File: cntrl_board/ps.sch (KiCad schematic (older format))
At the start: 52 parts, among them J10 PRI_TRF_L, J11 PRI_TRF_N, J12 SEC_OUT_L, J13 SEC_OUT_N, J6 MAIN_PWR_L, J7 MAIN_PWR_N, J8 SEC_TRF_L, J9 SEC_TRF_N, U1 LM2596S-ADJ, U17 LM1085-ADJ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

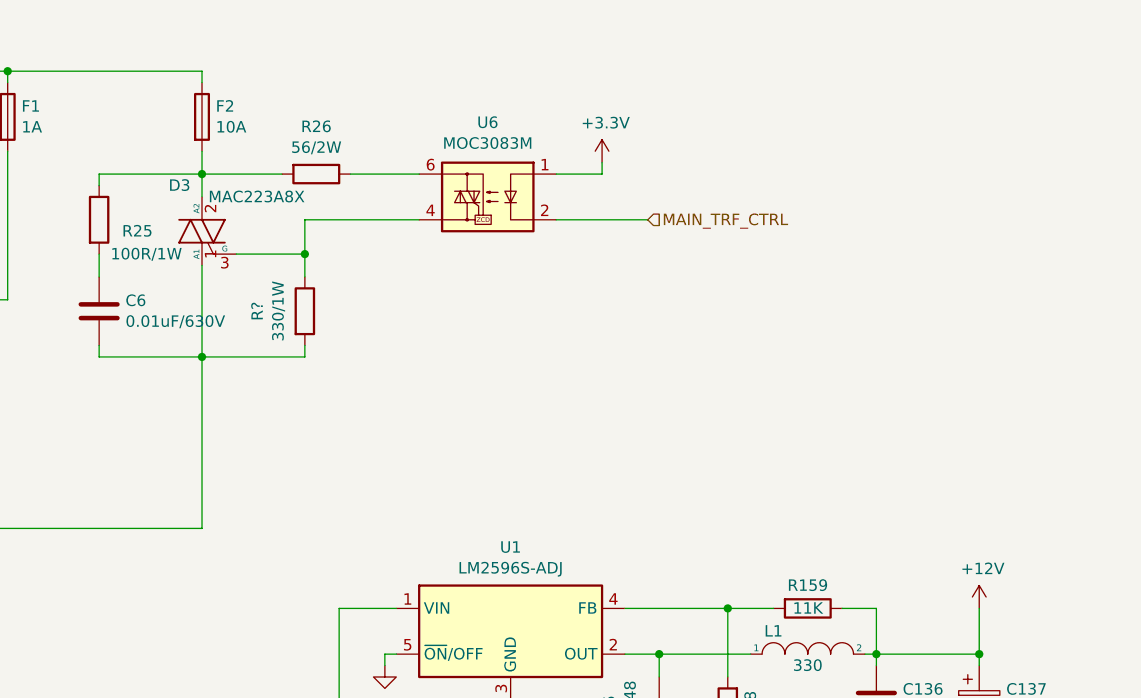
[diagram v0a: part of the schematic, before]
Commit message: update xformer soft startup
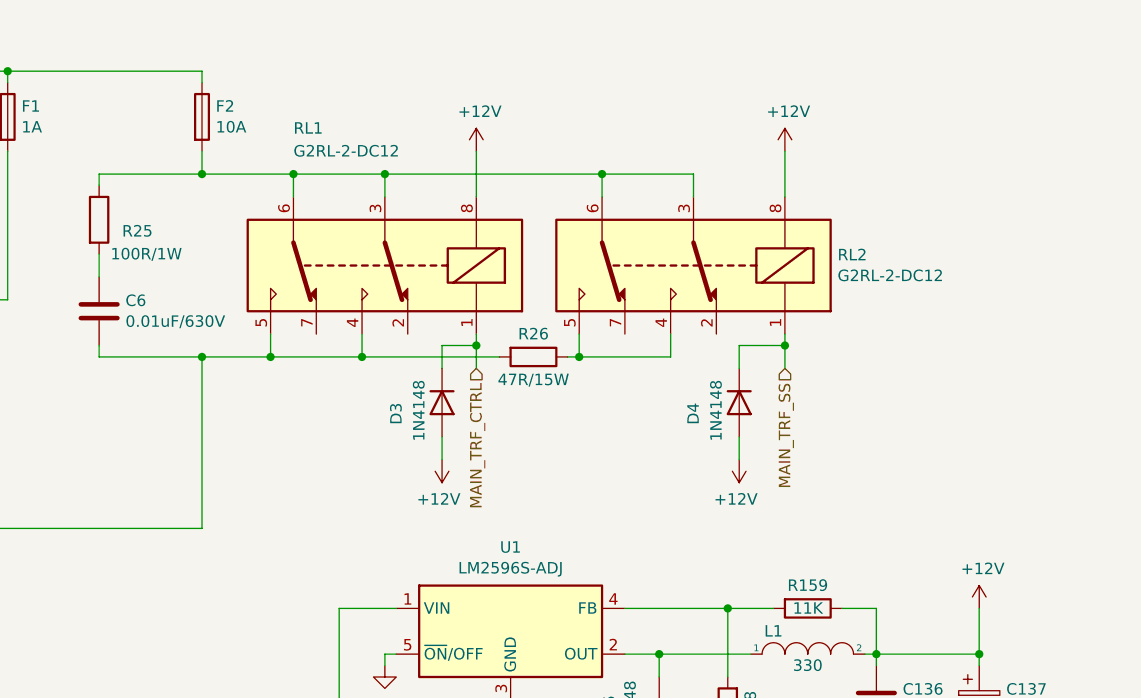
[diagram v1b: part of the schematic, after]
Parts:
- removed D3: MAC223A8X, Package_TO_SOT_THT:TO-220-3_Vertical, symbol Device:Q_TRIAC_A1A2G
- removed R?: 330/1W, Resistor_THT:R_Axial_DIN0414_L11.9mm_D4.5mm_P15.24mm_Horizontal, symbol Device:R
- removed U6: MOC3083M, symbol Relay_SolidState:MOC3083M
- added D3, D4: 1N4148, Diode_SMD:D_SOD-323_HandSoldering, symbol Device:D
- added RL1, RL2: G2RL-2-DC12, Relay_THT:Relay_DPDT_Omron_G2RL, symbol Relay:G2RL-2-DC12
- R26: value 56/2W -> 47R/15W; footprint Resistor_THT:R_Axial_DIN0414_L11.9mm_D4.5mm_P15.24mm_Horizontal -> Resistor_THT:R_Radial_Power_L13.0mm_W9.0mm_P5.00mm
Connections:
- net +12V: now also D3.2 (A), D4.2 (A), RL1.8, RL2.8
- net MAIN_TRF_CTRL: now also D3.1 (K), RL1.1
- net at C6.2, J10.1 (Pin_1): now also R26.2, RL1.4, RL1.5
- net at F2.2, R25.1: now also RL1.3, RL1.6, RL2.3, RL2.6; no longer R26.2
- net at R26.1: now also RL2.4, RL2.5
- new net MAIN_TRF_SS: D4.1 (K), RL2.1
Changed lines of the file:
@@
 $EndDescr
-$Comp
-L Device:Q_TRIAC_A1A2G D3
-U 1 1 60BF28E5
-P 2850 1750
-F 0 "D3" H 2900 1950 50  0000 L CNN
-F 1 "MAC223A8X" H 2400 1900 50  0000 L CNN
-F 2 "Package_TO_SOT_THT:TO-220-3_Vertical" V 2925 1775 50  0001 C CNN
-F 3 "~" V 2850 1750 50  0001 C CNN
-	1    2850 1750
-	-1   0    0    -1
-$EndComp
 $Comp
 L Connector:Conn_01x01_Male J10
@@
 	1    0    0    -1
 $EndComp
-Connection ~ 2850 1500
-Wire Wire Line
-	2850 1500 2850 1600
 Wire Wire Line
 	2400 1850 2400 1950
@@
 	2400 2250 2400 2300
 Wire Wire Line
-	2850 1900 2850 2300
-Wire Wire Line
 	2850 3050 2850 2300
 Wire Wire Line
 	1450 3050 2850 3050
-Connection ~ 2850 2300
 Wire Wire Line
 	2400 2300 2850 2300
@@
 Wire Wire Line
 	2400 1500 2850 1500
-$Comp
-L Device:R R26
-U 1 1 60C0976D
-P 3350 1500
-F 0 "R26" V 3143 1500 50  0000 C CNN
-F 1 "56/2W" V 3234 1500 50  0000 C CNN
-F 2 "Resistor_THT:R_Axial_DIN0414_L11.9mm_D4.5mm_P15.24mm_Horizontal" V 3280 1500 50  0001 C CNN
-F 3 "~" H 3350 1500 50  0001 C CNN
-	1    3350 1500
-	0    1    1    0
-$EndComp
-Wire Wire Line
-	2850 1500 3200 1500
-Wire Wire Line
-	4400 1700 4800 1700
 $Comp
 L Connector:Conn_01x01_Male J12
@@
 	1    0    0    -1
 $EndComp
-Text HLabel 4800 1700 2    50   Input ~ 0
+Text HLabel 4050 2350 3    50   Input ~ 0
 MAIN_TRF_CTRL
 $Comp
@@
 	9500 4950 9650 4950
 $Comp
-L power:+3.3V #PWR0266
-U 1 1 635ACB53
-P 4600 1450
-F 0 "#PWR0266" H 4600 1300 50  0001 C CNN
-F 1 "+3.3V" H 4615 1623 50  0000 C CNN
-F 2 "" H 4600 1450 50  0001 C CNN
-F 3 "" H 4600 1450 50  0001 C CNN
-	1    4600 1450
-	1    0    0    -1
-$EndComp
-Wire Wire Line
-	4600 1500 4600 1450
-Wire Wire Line
-	4400 1500 4600 1500
-$Comp
 L power:GND #PWR0135
 U 1 1 60E0C973
@@
 Wire Wire Line
 	4500 6100 4500 6250
-$Comp
-L Relay_SolidState:MOC3083M U6
-U 1 1 614D1E72
-P 4100 1600
-F 0 "U6" H 4100 1925 50  0000 C CNN
-F 1 "MOC3083M" H 4100 1834 50  0000 C CNN
-F 2 "" H 3900 1400 50  0001 L CIN
-F 3 "https://www.onsemi.com/pub/Collateral/MOC3083M-D.PDF" H 4100 1600 50  0001 L CNN
-	1    4100 1600
-	-1   0    0    -1
-$EndComp
-$Comp
-L Device:R R?
-U 1 1 61538D39
-P 3300 2100
-F 0 "R?" V 3093 2100 50  0000 C CNN
-F 1 "330/1W" V 3184 2100 50  0000 C CNN
-F 2 "Resistor_THT:R_Axial_DIN0414_L11.9mm_D4.5mm_P15.24mm_Horizontal" V 3230 2100 50  0001 C CNN
-F 3 "~" H 3300 2100 50  0001 C CNN
-	1    3300 2100
-	1    0    0    -1
-$EndComp
-Wire Wire Line
-	3000 1850 3300 1850
-Wire Wire Line
-	3500 1500 3800 1500
-Wire Wire Line
-	2850 2300 3300 2300
-Wire Wire Line
-	3300 2300 3300 2250
-Wire Wire Line
-	3300 1950 3300 1850
-Connection ~ 3300 1850
-Wire Wire Line
-	3300 1850 3300 1700
-Wire Wire Line
-	3300 1700 3800 1700
+Text HLabel 5400 2350 3    50   Input ~ 0
+MAIN_TRF_SS
+$Comp
+L Relay:G2RL-2-DC12 RL1
+U 1 1 616FA480
+P 3650 1900
+F 0 "RL1" H 4050 1300 50  0000 R CNN
+F 1 "G2RL-2-DC12" H 4050 1400 50  0000 R CNN
+F 2 "Relay_THT:Relay_DPDT_Omron_G2RL" H 4300 1850 50  0001 L CNN
+F 3 "https://omronfs.omron.com/en_US/ecb/products/pdf/en-g2rl.pdf" H 3650 1900 50  0001 C CNN
+	1    3650 1900
+	-1   0    0    1
+$EndComp
+Wire Wire Line
+	2850 2300 3150 2300
+Wire Wire Line
+	3150 2300 3150 2200
+Connection ~ 2850 2300
+Wire Wire Line
+	3150 2300 3550 2300
+Wire Wire Line
+	3550 2300 3550 2200
+Connection ~ 3150 2300
+Wire Wire Line
+	2850 1500 3250 1500
+Wire Wire Line
+	3650 1500 3650 1600
+Connection ~ 2850 1500
+Wire Wire Line
+	3250 1600 3250 1500
+Connection ~ 3250 1500
+Wire Wire Line
+	3250 1500 3650 1500
+$Comp
+L Relay:G2RL-2-DC12 RL2
+U 1 1 617224A5
+P 5000 1900
+F 0 "RL2" H 4370 1854 50  0000 R CNN
+F 1 "G2RL-2-DC12" H 4370 1945 50  0000 R CNN
+F 2 "Relay_THT:Relay_DPDT_Omron_G2RL" H 5650 1850 50  0001 L CNN
+F 3 "https://omronfs.omron.com/en_US/ecb/products/pdf/en-g2rl.pdf" H 5000 1900 50  0001 C CNN
+	1    5000 1900
+	-1   0    0    1
+$EndComp
+Wire Wire Line
+	3650 1500 4600 1500
+Wire Wire Line
+	5000 1500 5000 1600
+Connection ~ 3650 1500
+Wire Wire Line
+	4600 1600 4600 1500
+Connection ~ 4600 1500
+Wire Wire Line
+	4600 1500 5000 1500
+$Comp
+L Device:R R26
+U 1 1 61740C83
+P 4300 2300
+F 0 "R26" V 4200 2300 50  0000 C CNN
+F 1 "47R/15W" V 4400 2300 50  0000 C CNN
+F 2 "Resistor_THT:R_Radial_Power_L13.0mm_W9.0mm_P5.00mm" V 4230 2300 50  0001 C CNN
+F 3 "~" H 4300 2300 50  0001 C CNN
+	1    4300 2300
+	0    1    1    0
+$EndComp
+Wire Wire Line
+	3550 2300 4150 2300
+Connection ~ 3550 2300
+Wire Wire Line
+	4900 2300 4900 2200
+Wire Wire Line
+	4450 2300 4500 2300
+Wire Wire Line
+	4500 2200 4500 2300
+Connection ~ 4500 2300
+Wire Wire Line
+	4500 2300 4900 2300
+Wire Wire Line
+	5400 2350 5400 2250
+Wire Wire Line
+	4050 2350 4050 2250
+$Comp
+L power:+12V #PWR0207
+U 1 1 617973F5
+P 5400 1400
+F 0 "#PWR0207" H 5400 1250 50  0001 C CNN
+F 1 "+12V" H 5415 1573 50  0000 C CNN
+F 2 "" H 5400 1400 50  0001 C CNN
+F 3 "" H 5400 1400 50  0001 C CNN
+	1    5400 1400
+	1    0    0    -1
+$EndComp
+$Comp
+L power:+12V #PWR0266
+U 1 1 6179DD42
+P 4050 1400
+F 0 "#PWR0266" H 4050 1250 50  0001 C CNN
+F 1 "+12V" H 4065 1573 50  0000 C CNN
+F 2 "" H 4050 1400 50  0001 C CNN
+F 3 "" H 4050 1400 50  0001 C CNN
+	1    4050 1400
+	1    0    0    -1
+$EndComp
+Wire Wire Line
+	4050 1600 4050 1400
+Wire Wire Line
+	5400 1400 5400 1600
+$Comp
+L Device:D D?
+U 1 1 618034AE
+P 3900 2500
+AR Path="/60BF25B5/618034AE" Ref="D?"  Part="1"
+AR Path="/60BF2601/618034AE" Ref="D3"  Part="1"
+F 0 "D3" H 3900 2300 50  0000 L CNN
+F 1 "1N4148" H 3800 2400 50  0000 L CNN
+F 2 "Diode_SMD:D_SOD-323_HandSoldering" H 3900 2500 50  0001 C CNN
+F 3 "~" H 3900 2500 50  0001 C CNN
+	1    3900 2500
+	0    1    1    0
+$EndComp
+$Comp
+L Device:D D?
+U 1 1 61809CDA
+P 5200 2500
+AR Path="/60BF25B5/61809CDA" Ref="D?"  Part="1"
+AR Path="/60BF2601/61809CDA" Ref="D4"  Part="1"
+F 0 "D4" H 5200 2300 50  0000 L CNN
+F 1 "1N4148" H 5100 2400 50  0000 L CNN
+F 2 "Diode_SMD:D_SOD-323_HandSoldering" H 5200 2500 50  0001 C CNN
+F 3 "~" H 5200 2500 50  0001 C CNN
+	1    5200 2500
+	0    1    1    0
+$EndComp
+Wire Wire Line
+	3900 2350 3900 2250
+Wire Wire Line
+	3900 2250 4050 2250
+Connection ~ 4050 2250
+Wire Wire Line
+	4050 2250 4050 2200
+Wire Wire Line
+	5200 2350 5200 2250
+Wire Wire Line
+	5200 2250 5400 2250
+Connection ~ 5400 2250
+Wire Wire Line
+	5400 2250 5400 2200
+$Comp
+L power:+12V #PWR0273
+U 1 1 6181EE52
+P 5200 2750
+F 0 "#PWR0273" H 5200 2600 50  0001 C CNN
+F 1 "+12V" H 5215 2923 50  0000 C CNN
+F 2 "" H 5200 2750 50  0001 C CNN
+F 3 "" H 5200 2750 50  0001 C CNN
+	1    5200 2750
+	-1   0    0    1
+$EndComp
+Wire Wire Line
+	5200 2650 5200 2750
+$Comp
+L power:+12V #PWR0274
+U 1 1 6182ED18
+P 3900 2750
+F 0 "#PWR0274" H 3900 2600 50  0001 C CNN
+F 1 "+12V" H 3915 2923 50  0000 C CNN
+F 2 "" H 3900 2750 50  0001 C CNN
+F 3 "" H 3900 2750 50  0001 C CNN
+	1    3900 2750
+	-1   0    0    1
+$EndComp
+Wire Wire Line
+	3900 2650 3900 2750
 $EndSCHEMATC
